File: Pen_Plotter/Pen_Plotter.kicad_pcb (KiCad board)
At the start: 2 copper layers, 37 parts, among them J1 USB_Type-C_Breakout, J2 PinHeader_01x05_P2.54mm_Verti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, J3 PinHeader_01x05_P2.54mm_Verti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, J4 Screw_Terminal_01x02_P3.5mm, J5 PinHeader_01x02_P2.54mm_Verti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, J6 PinHeader_01x02_P2.54mm_Verti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, J7 PinHeader_01x03_P2.54mm_Verti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, Q1 Transistor_MOSFET_NCh_SOT23, Q2 Transistor_MOSFET_NCh_SOT23, SW1 Switch_Tactile_Omron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

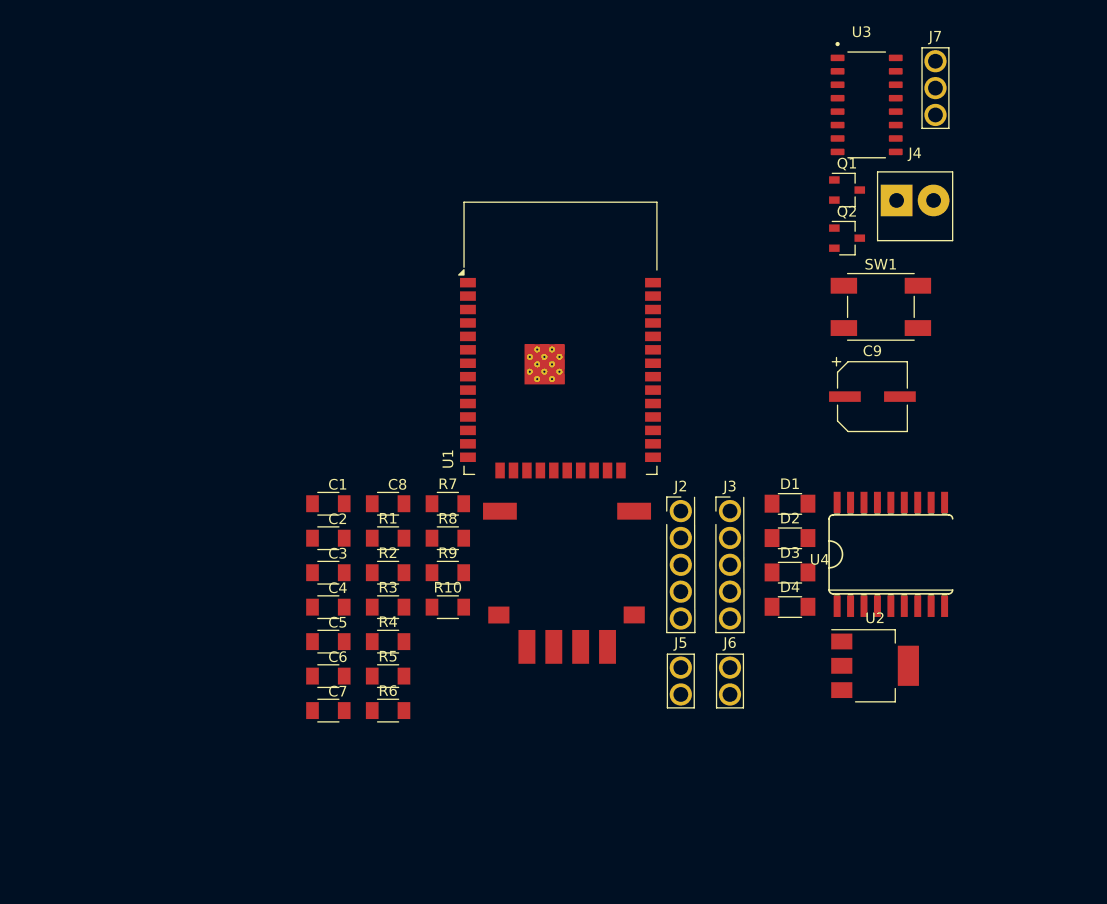
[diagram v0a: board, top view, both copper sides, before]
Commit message: Wired THT Components
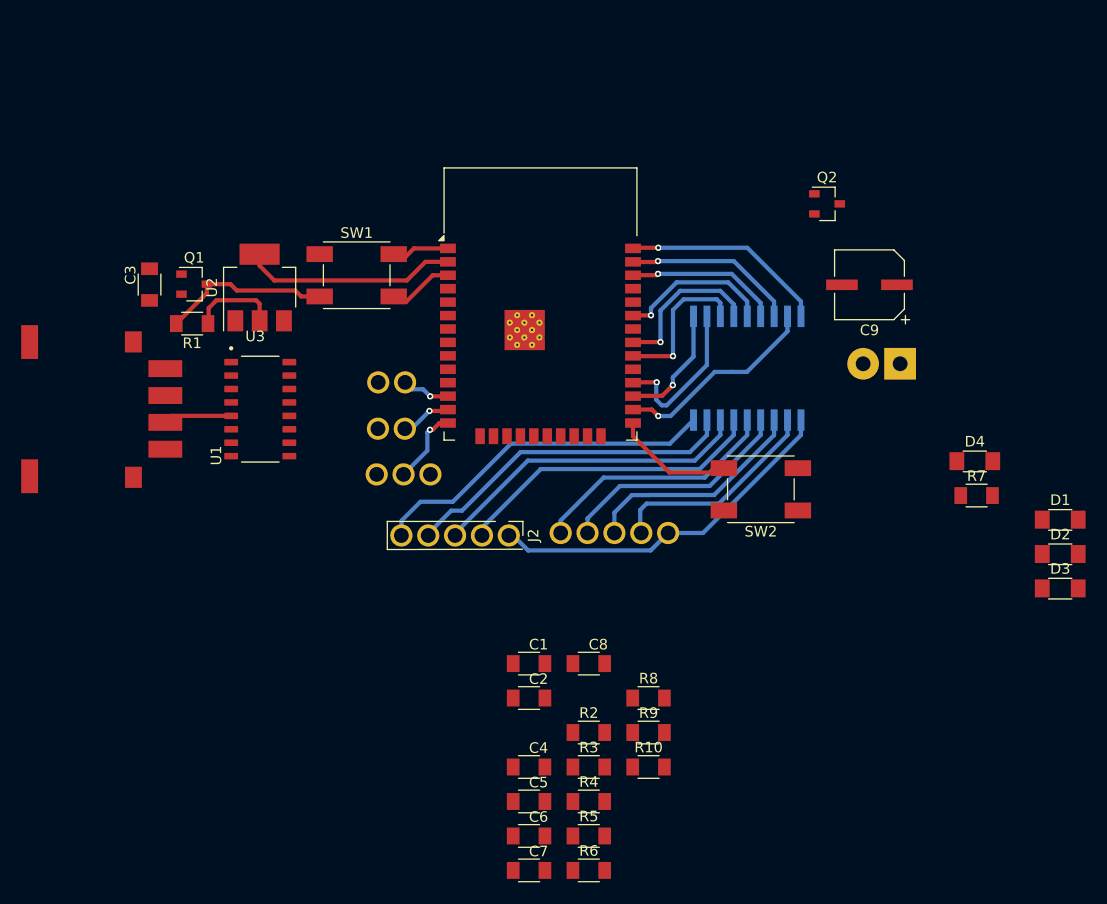
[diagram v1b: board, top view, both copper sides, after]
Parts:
- added SW2: Switch_Tactile_Omron, fab:Button_Omron_B3SN_6.0x6.0mm, F.Cu at (164.0, 93.2)
- J3, J4, J5, J6, J7, U4: moved to B.Cu
- moved U2 68.3 mm to (116.6, 74.1), turned to 90 degrees
- moved U3 64.2 mm to (116.7, 85.6)
- moved Q1 62.4 mm to (110.4, 73.8)
- moved J7 61.7 mm to (132.8, 91.8), turned to 90 degrees
- moved R7 50.0 mm to (184.4, 93.8)
- moved SW1 49.7 mm to (125.8, 72.9)
- moved J1 44.2 mm to (107.7, 85.6), turned to 90 degrees
- moved J6 40.9 mm to (130.4, 83.1), turned to 90 degrees
- moved J5 34.5 mm to (130.3, 87.5), turned to 90 degrees
- moved C3 32.1 mm to (106.2, 73.8), turned to 90 degrees
- moved R1 27.5 mm to (110.2, 77.5), turned to 180 degrees
- moved D1 25.6 mm to (192.3, 96.0)
- moved D2 25.6 mm to (192.3, 99.3)
- moved D3 25.6 mm to (192.3, 102.5)
- moved R2 24.3 mm to (147.7, 116.2)
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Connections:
- U1 pad 10: IN8 -> unconnected-(U1-IO25-Pad10)
- U1 pad 12: unconnected-(U1-IO27-Pad12) -> X Lim
- U1 pad 13: unconnected-(U1-IO14-Pad13) -> Y Lim
- U1 pad 14: unconnected-(U1-IO12-Pad14) -> Servo
- U1 pad 26: unconnected-(U1-IO4-Pad26) -> IN8
- U1 pad 6: Y Lim -> unconnected-(U1-IO34-Pad6)
- U1 pad 7: X Lim -> unconnected-(U1-IO35-Pad7)
- U1 pad 8: Servo -> unconnected-(U1-IO32-Pad8)
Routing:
- net PWR_5V: track 0.00 -> 34.1 mm
- net OUT1: track 0.00 -> 33.0 mm
- net OUT2: track 0.00 -> 32.4 mm
- net OUT3: track 0.00 -> 30.6 mm
- net OUT4: track 0.00 -> 29.6 mm
- net VDD: track 0.00 -> 28.6 mm
- net PWR_GND: track 0.00 -> 25.0 mm, vias 0 -> 1
- net OUT5: track 0.00 -> 23.6 mm
- net EN: track 0.00 -> 22.5 mm
- net OUT6: track 0.00 -> 22.4 mm
- net OUT7: track 0.00 -> 21.5 mm
- net OUT8: track 0.00 -> 20.5 mm
- net IN8: track 0.00 -> 19.6 mm, vias 0 -> 1
- net IN7: track 0.00 -> 16.4 mm, vias 0 -> 1
- net IN2: track 0.00 -> 15.1 mm, vias 0 -> 1
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
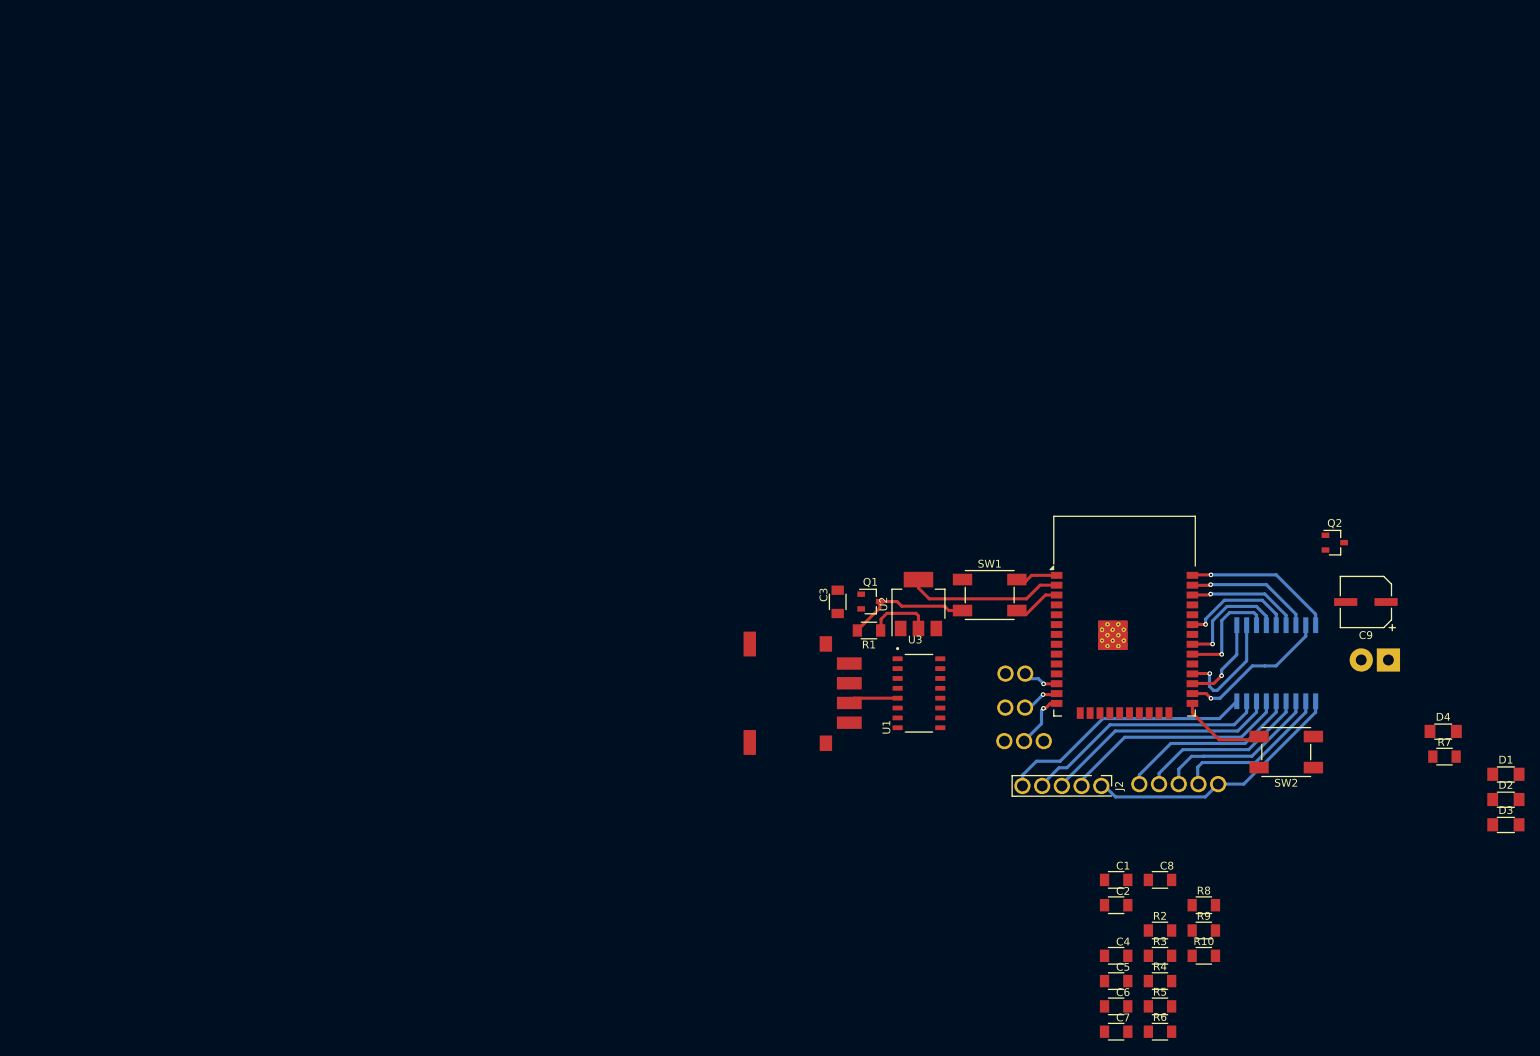
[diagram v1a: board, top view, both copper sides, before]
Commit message: Version with Auto Programmer, USBC and CH340 IC
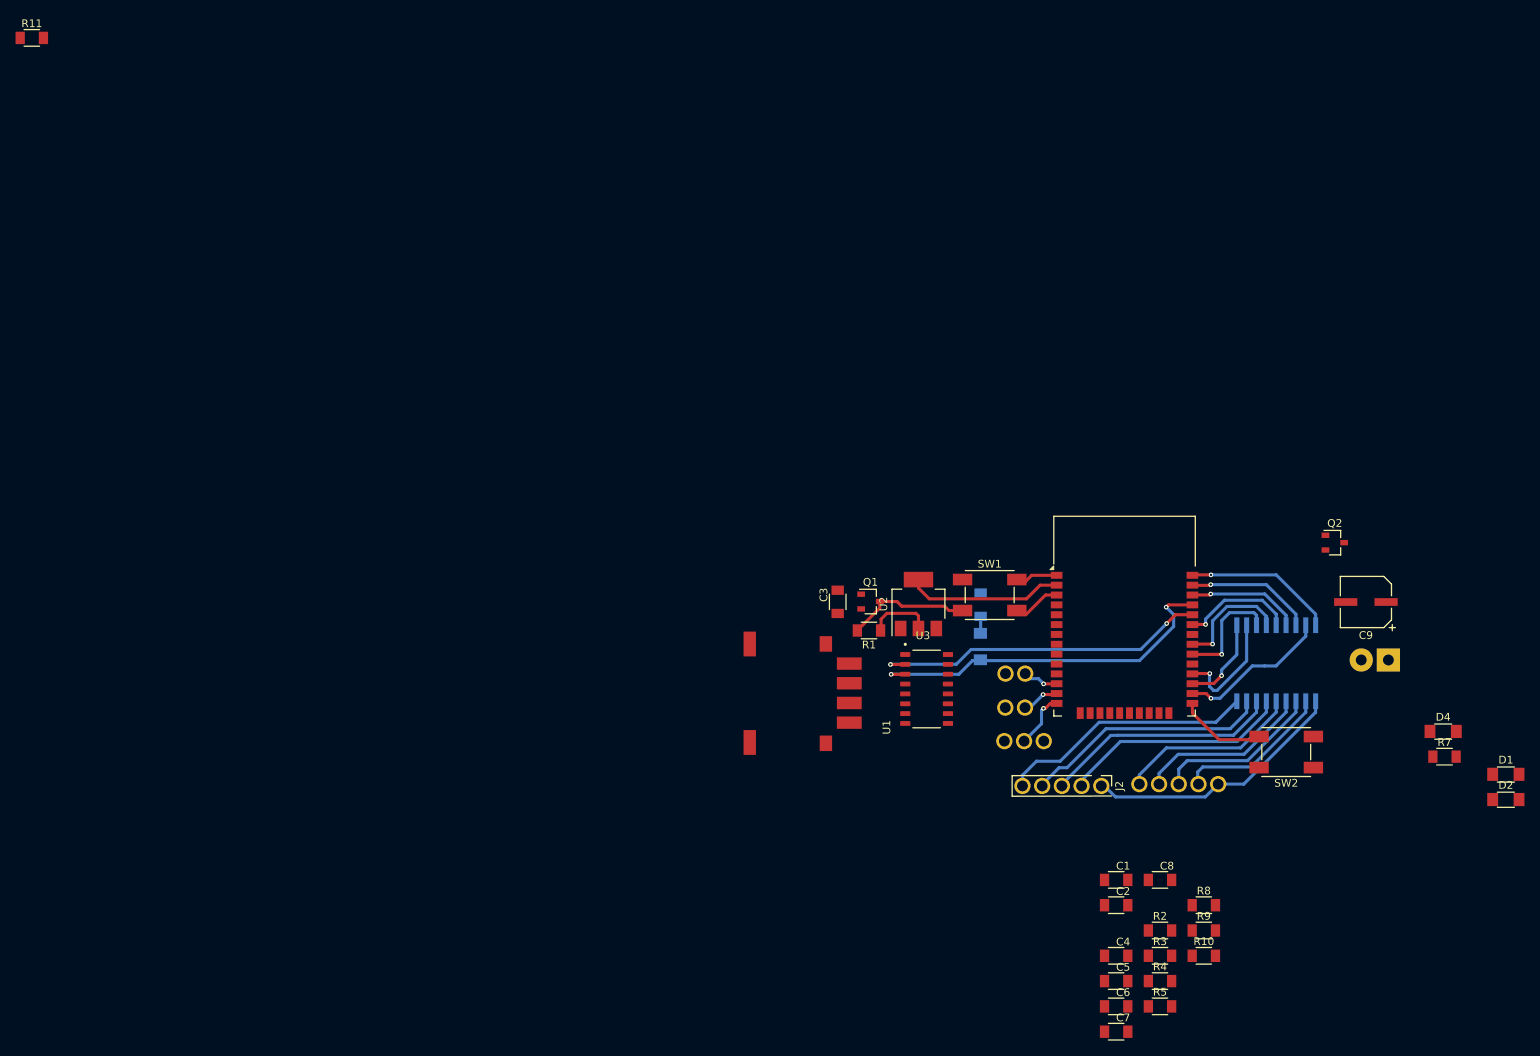
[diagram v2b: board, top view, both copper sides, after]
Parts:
- added R11: 10K, fab:R_1206, F.Cu at (2.33, 1.13)
- D3, R6: moved to B.Cu
- moved D3 71.5 mm to (124.6, 79.6), turned to 90 degrees
- moved R6 59.7 mm to (124.6, 74.2), turned to -90 degrees
- moved U3 1.13 mm to (117.7, 85.0)
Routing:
- net TX: track 0.00 -> 47.2 mm, vias 0 -> 2
- net RX: track 0.00 -> 43.5 mm, vias 0 -> 2
- net D+: track 6.48 -> 0.00 mm
- net Net-(D3-A): track 0.00 -> 2.20 mm

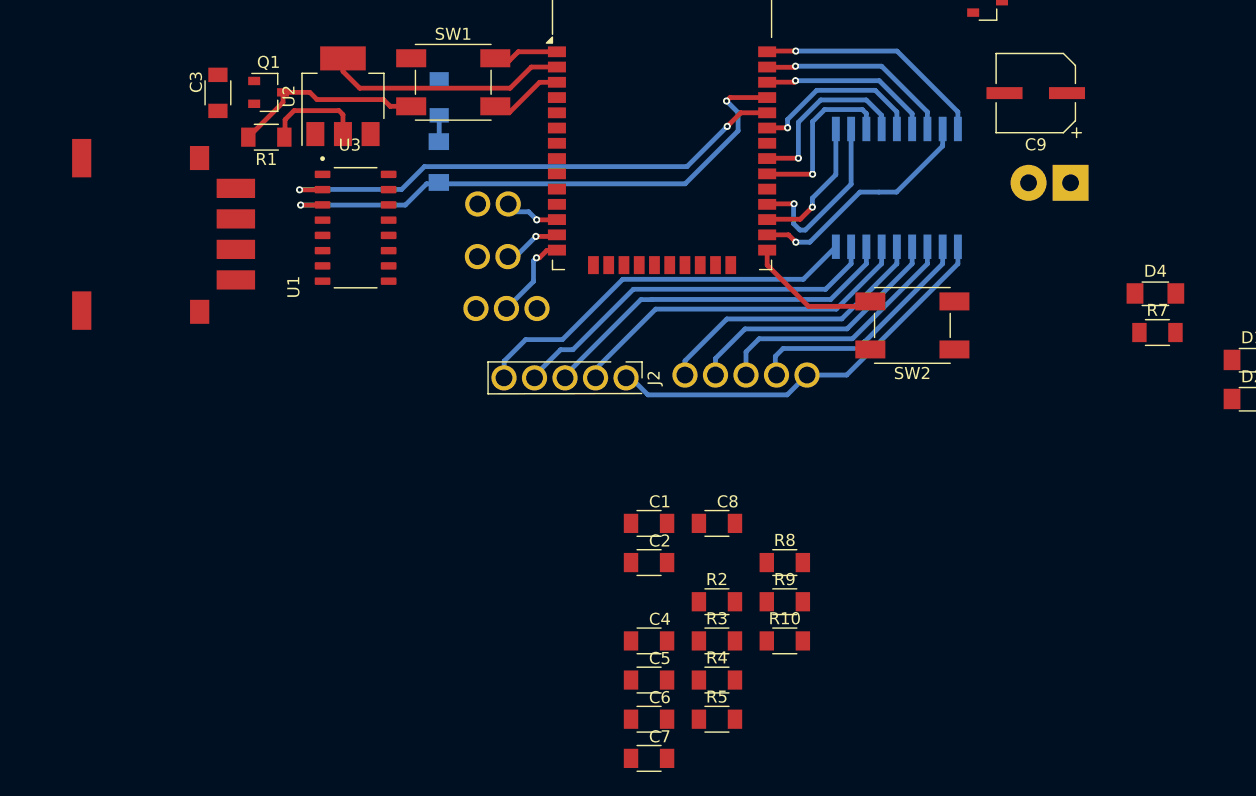
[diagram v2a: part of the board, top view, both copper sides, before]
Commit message: Schematic Excluded USBC, CH340IC, Autoprogrammer PCB: Removed components
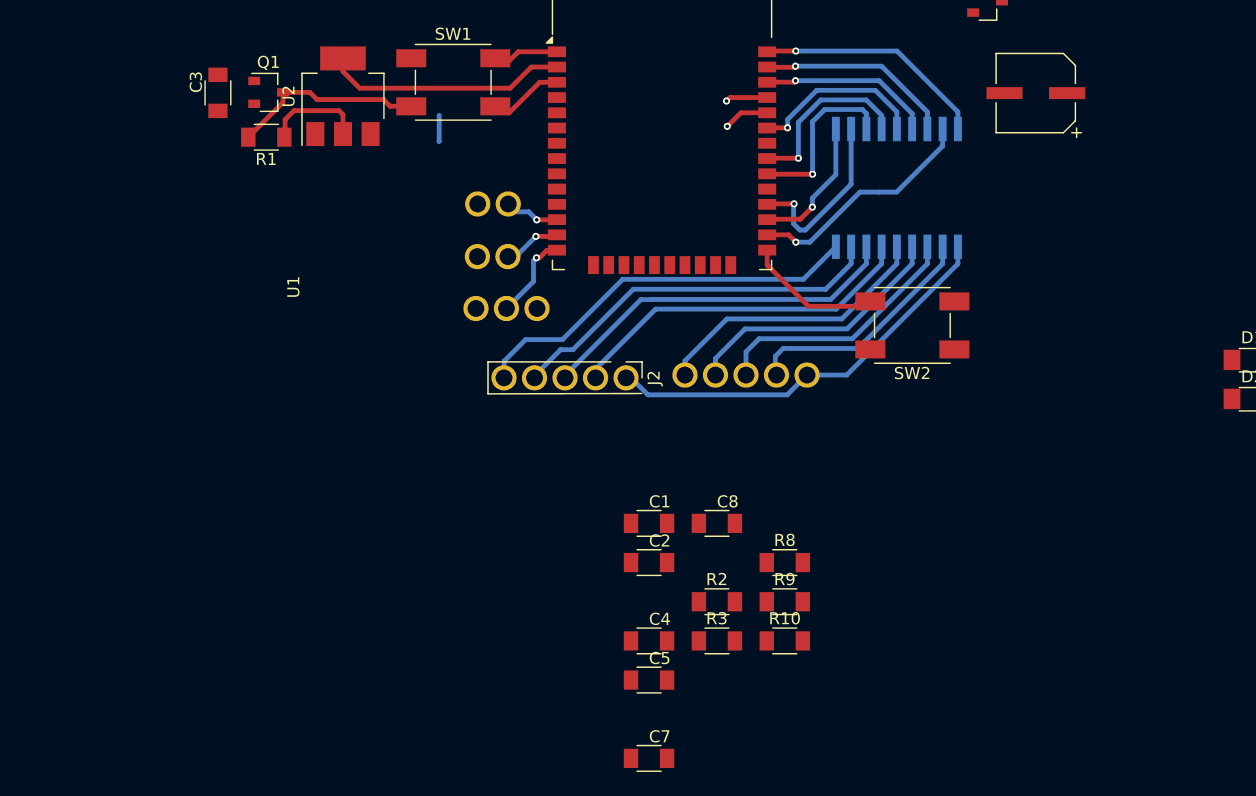
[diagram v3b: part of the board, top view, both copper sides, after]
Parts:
- removed C6: 22uF, fab:C_1206
- removed D3, D4: Green, fab:LED_1206
- removed J1: USB_Type-C_Breakout, Proshplay Type C:ProshPlay-Type-C-breakout-board
- removed J4: Screw_Terminal_01x02_P3.5mm, fab:TerminalBlock_OnShore_1x02_P3.50mm_Horizontal
- removed R4, R5: 10K, fab:R_1206
- removed R6, R7: 500, fab:R_1206
- removed U3: CH340C, CH340C:SOIC127P600X180-16N
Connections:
- U1 pad 14: Servo -> GPIO12
- U1 pad 16: unconnected-(U1-IO13-Pad16) -> Servo
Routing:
- net TX: track 47.2 -> 3.50 mm, vias 2 -> 1
- net RX: track 43.5 -> 3.79 mm, vias 2 -> 1

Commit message: PCB for ESP UCap
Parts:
- removed Q1, Q2: Transistor_MOSFET_NCh_SOT23, fab:SOT-23-3
- added J4: Conn_02x03_Counter_Clockwise, Connector_PinHeader_2.54mm:PinHeader_2x03_P2.54mm_Horizontal, F.Cu at (106.3, 102.5)
- added R4: 10K, fab:R_1206, F.Cu at (72.8, 101.3)
- added R5: 10K, fab:R_1206, F.Cu at (65.2, 109.7)
- added R6: 0, fab:R_1206, F.Cu at (99.2, 99.3)
- J3, J5, J6, J7, U4: moved to F.Cu
- moved R11 141.6 mm to (78.4, 120.5), turned to 90 degrees
- moved D2 132.4 mm to (60.5, 111.4), turned to 90 degrees
- moved D1 102.7 mm to (93.0, 122.5), turned to 90 degrees
- moved R3 88.3 mm to (60.5, 105.6), turned to -90 degrees
- moved C8 82.7 mm to (65.4, 117.3)
- moved R10 80.8 mm to (73.5, 107.6), turned to 180 degrees
- moved R9 80.1 mm to (73.5, 110.9), turned to 180 degrees
- moved C4 78.4 mm to (65.2, 104.1), turned to 180 degrees
- moved C7 77.3 mm to (65.4, 120.1)
- moved R8 75.0 mm to (78.4, 116.0)
- moved C2 72.4 mm to (71.5, 97.0), turned to -90 degrees
- moved C5 71.6 mm to (72.8, 104.7)
- moved C1 69.0 mm to (74.3, 97.0), turned to -90 degrees
- moved J6 68.2 mm to (70.2, 115.3), turned to 0 degrees
- moved SW2 66.5 mm to (103.7, 121.1), turned to -90 degrees
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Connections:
- U1 pad 27: IN1 -> IN7
- U1 pad 28: IN2 -> IN6
- U1 pad 30: IN3 -> IN5
- U1 pad 33: IN5 -> IN3
- U1 pad 36: IN6 -> IN2
- U1 pad 37: IN7 -> IN1
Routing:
- net PWR_5V: track 34.1 -> 0.00 mm
- net OUT1: track 33.0 -> 0.00 mm
- net OUT2: track 32.4 -> 0.00 mm
- net OUT3: track 30.6 -> 0.00 mm
- net OUT4: track 29.6 -> 0.00 mm
- net VDD: track 28.6 -> 0.00 mm
- net PWR_GND: track 25.0 -> 0.00 mm, vias 1 -> 0
- net OUT5: track 23.6 -> 0.00 mm
- net EN: track 22.5 -> 0.00 mm
- net OUT6: track 22.4 -> 0.00 mm
- net OUT7: track 21.5 -> 0.00 mm
- net OUT8: track 20.1 -> 0.00 mm
- net IN8: track 19.6 -> 0.00 mm, vias 1 -> 0
- net IN7: track 16.4 -> 0.00 mm, vias 1 -> 0
- net IN2: track 15.1 -> 0.00 mm, vias 1 -> 0
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
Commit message: Mini Plotter PCB 13
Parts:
- removed R5: 10K, fab:R_1206
- added J1: USB4125-GF-A_REVA2, USB4125-GF-A_REVA2:GCT_USB4125-GF-A_REVA2, F.Cu at (74.3, 124.2)
- added R7: 0, fab:R_1206, F.Cu at (103.6, 104.7)
- moved C9 86.9 mm to (59.5, 121.4), turned to -90 degrees
- moved J2 13.9 mm to (121.5, 111.0), turned to 0 degrees
- moved R8 11.8 mm to (90.2, 116.7), turned to 90 degrees
- moved R11 4.69 mm to (78.4, 115.8)
- moved J3 2.82 mm to (114.7, 121.2)
- moved C3 2.05 mm to (64.9, 111.0)
- moved C8 1.92 mm to (65.4, 115.3)
- moved U4 1.79 mm to (117.8, 101.0)
- moved C1 1.34 mm to (73.0, 97.2)
- moved C2 1.34 mm to (70.2, 97.2)
- moved SW1 1.26 mm to (103.6, 111.5)
- moved J4 1.19 mm to (105.4, 101.8)
- moved R1 1.12 mm to (64.9, 107.7)
- moved SW2 0.96 mm to (103.6, 122.0)
- moved U2 0.89 mm to (65.0, 98.9)
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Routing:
- net PWR_5V: track 0.00 -> 141.4 mm
- net GPIO0: track 0.00 -> 134.1 mm, vias 0 -> 2
- net PWR_GND: track 0.00 -> 105.5 mm, vias 0 -> 3
- net VDD: track 0.00 -> 69.3 mm, vias 0 -> 2
- net EN: track 0.00 -> 59.3 mm, vias 0 -> 1
- net IN8: track 0.00 -> 43.1 mm
- net IN4: track 0.00 -> 31.0 mm
- net OUT1: track 0.00 -> 30.3 mm
- net IN5: track 0.00 -> 30.2 mm
- net IN6: track 0.00 -> 28.1 mm
- net IN7: track 0.00 -> 26.9 mm
- net OUT2: track 0.00 -> 25.9 mm
- net IN3: track 0.00 -> 25.8 mm
- net OUT3: track 0.00 -> 21.3 mm
- net IN2: track 0.00 -> 18.6 mm
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- added copper zone on F.Cu, net PWR_GND
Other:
- board outline added: 73.6 x 36.3 mm

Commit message: Added gerber files
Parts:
- added H1: ~, fab:MountingHole_M3, F.Cu at (127.6, 124.0)
- added H2: ~, fab:MountingHole_M3, F.Cu at (127.6, 94.7)
- added H3: ~, fab:MountingHole_M3, F.Cu at (58.6, 94.7)
- added H4: ~, fab:MountingHole_M3, F.Cu at (87.4, 124.5)
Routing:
- net PWR_GND: track 105.5 -> 109.1 mm
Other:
- board size 73.6 x 36.3 mm -> 74.8 x 35.8 mm

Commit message: First PCB Final - Problems with RX-TX
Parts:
- C3: value C_1206 -> 1uF
- C4, C5: value 22uF -> 10uF
- C8: value C_1206 -> 0.1uF
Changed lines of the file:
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@@
 			)
 		)
-		(property "Value" "22uF"
+		(property "Value" "10uF"
 			(at 0 1.9 0)
 			(layer "F.Fab")
@@
 			)
 		)
-		(property "Value" "C_1206"
+		(property "Value" "1uF"
 			(at 0 1.9 0)
 			(layer "F.Fab")
@@
 			)
 		)
-		(property "Value" "22uF"
+		(property "Value" "10uF"
 			(at 0 1.9 0)
 			(layer "F.Fab")
@@
 			)
 		)
-		(property "Value" "C_1206"
+		(property "Value" "0.1uF"
 			(at 0 1.9 0)
 			(layer "F.Fab")
